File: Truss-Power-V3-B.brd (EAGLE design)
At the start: 40.3 x 20.3 mm, 41 parts, among them J1 XF2L-0625-1, U1 TPS61090, U2 MCP73831T-2ACI/OT, U3 MAX17044, U4 SN74LVC1G86DC1LR, U5 SN74LVC1G123, X1 CON-1PIN, X2 MicroB, X3 CON-1PINB, X4 CON-1PIN, X5 CON-1PIN, X6 CON-1PIN

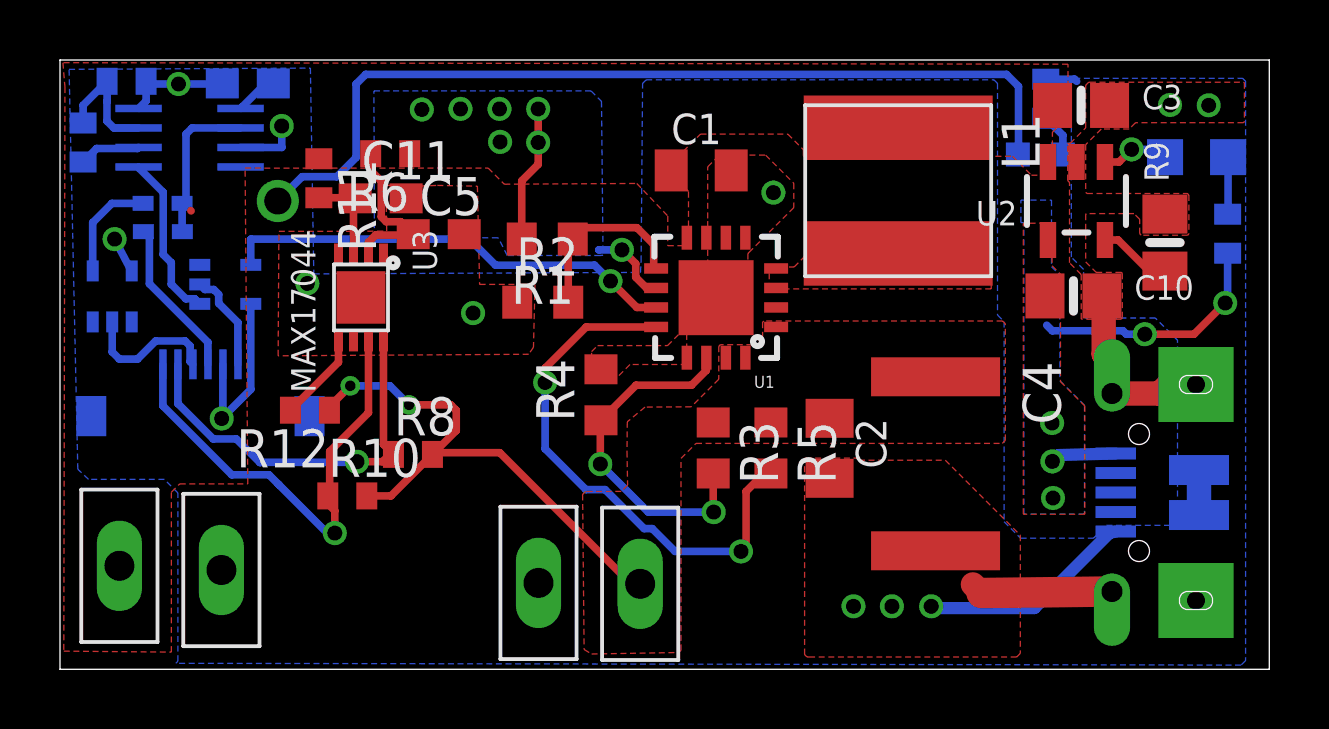
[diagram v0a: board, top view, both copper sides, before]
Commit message: Decoupling capacitor added to XOR power supply
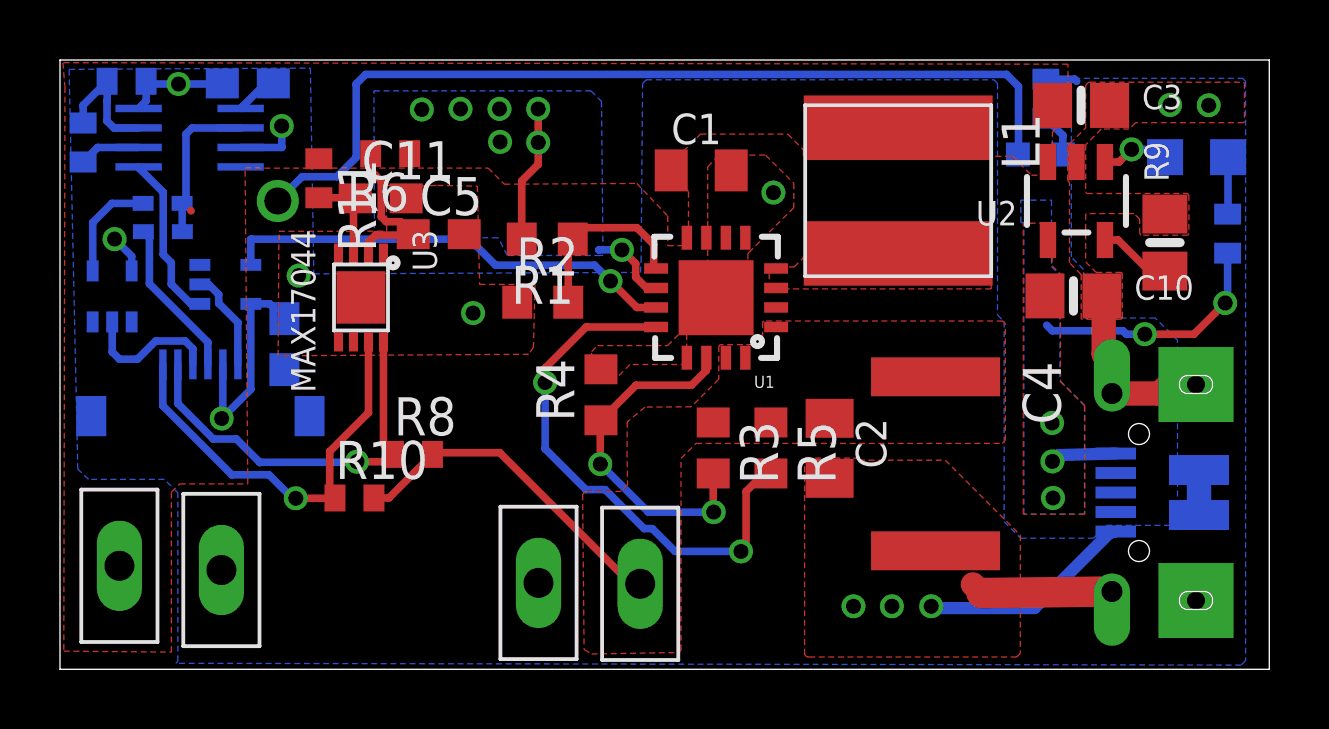
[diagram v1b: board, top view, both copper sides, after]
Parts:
- removed R12: 4.7K, resistor:R0402
- added C8: 0.1uF, rcl:C0603
- moved R10 0.25 mm to (9.82, 5.71)
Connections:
- removed net ALRT: R12.2, U3.5
- net GND: now also C8.2, U5.1, U5.4; no longer U5.P$1, U5.P$4
- net N$10: now also U5.6; no longer U5.P$6
- net N$8: now also U5.7; no longer U5.P$7
- net N$9: now also U5.2; no longer U5.P$2
- net PWR_OR_R: now also U5.5; no longer U5.P$5
- net VBAT: now also C8.1, U5.3, U5.8; no longer U5.P$3, U5.P$8
- net VCC: no longer R12.1
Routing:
- net VCC: track 18.0 -> 11.0 mm, vias 2 -> 0
- net ALRT: track 2.97 -> 0.00 mm
- net SCL: track 16.1 -> 14.2 mm
- net VBAT: track 20.3 -> 21.8 mm

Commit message: Final board files
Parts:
- R13: value 330 -> 1K
- moved C7 1.31 mm to (4.95, 19.5)
- moved R14 0.89 mm to (1.33, 19.6)
- moved C6 0.30 mm to (0.76, 17.3)
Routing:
- net VBAT: track 21.8 -> 20.5 mm
- net N$8: track 4.20 -> 3.60 mm
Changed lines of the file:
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@@
 <?xml version="1.0" encoding="utf-8"?>
 <!DOCTYPE eagle SYSTEM "eagle.dtd">
-<eagle version="8.3.2">
+<eagle version="8.4.3">
 <drawing>
 <settings>
@@
 <param name="dpMaxLengthDifference" value="10mm"/>
 <param name="dpGapFactor" value="2.5"/>
-<param name="checkGrid" value="0"/>
 <param name="checkAngle" value="0"/>
 <param name="checkFont" value="1"/>
 <param name="checkRestrict" value="0"/>
+<param name="checkStop" value="0"/>
 <param name="useDiameter" value="13"/>
 <param name="maxErrors" value="50"/>
@@
 <element name="C5" library="rcl" package="C0603" value="1uF" x="12.6238" y="14.5034"/>
 <element name="LED1" library="led" library_urn="urn:adsk.eagle:library:259" package="CHIP-LED0603" package3d_urn="urn:adsk.eagle:package:15819/1" value="" x="32.68" y="17.16" rot="MR90"/>
-<element name="R13" library="resistor" package="R0402" value="330" x="32.86" y="19.02" rot="MR270"/>
+<element name="R13" library="resistor" package="R0402" value="1K" x="32.86" y="19.02" rot="MR270"/>
 <element name="R7" library="resistor" package="R0402" value="470" x="38.92" y="14.52" rot="MR90"/>
 <element name="X4" library="NewPart" package="CON-1PIN" value="CON-1PIN" x="1.98" y="3.45" rot="R180"/>
@@
 <element name="X3" library="NewPart" package="CON-1PIN-B" value="CON-1PINB" x="7.26" y="15.61"/>
 <element name="U5" library="NewPart" package="SSOP8" value="SN74LVC1G123" x="4.32" y="17.72" rot="MR270"/>
-<element name="R14" library="resistor" package="R0402" value="10K" x="2.22" y="19.6" rot="MR0"/>
-<element name="C6" library="rcl" library_urn="urn:adsk.eagle:library:334" package="C0402" package3d_urn="urn:adsk.eagle:package:23626/1" value="1000pF" x="0.77" y="17.56" rot="MR270"/>
-<element name="C7" library="rcl" library_urn="urn:adsk.eagle:library:334" package="C0603" package3d_urn="urn:adsk.eagle:package:23616/2" value="0.1uF" x="6.26" y="19.53" rot="MR180"/>
+<element name="R14" library="resistor" package="R0402" value="10K" x="1.33" y="19.56" rot="MR0"/>
+<element name="C6" library="rcl" library_urn="urn:adsk.eagle:library:334" package="C0402" package3d_urn="urn:adsk.eagle:package:23626/1" value="1000pF" x="0.76" y="17.26" rot="MR270"/>
+<element name="C7" library="rcl" library_urn="urn:adsk.eagle:library:334" package="C0603" package3d_urn="urn:adsk.eagle:package:23616/2" value="0.1uF" x="4.95" y="19.49" rot="MR180"/>
 <element name="C8" library="rcl" library_urn="urn:adsk.eagle:library:334" package="C0603" package3d_urn="urn:adsk.eagle:package:23616/2" value="0.1uF" x="7.48" y="10.84" rot="MR270"/>
 </elements>
@@
 <wire x1="6.02" y1="18.695" x2="6.0756" y2="18.7506" width="0.254" layer="16"/>
 <wire x1="6.0756" y1="18.7506" x2="6.07573125" y2="18.7506" width="0.254" layer="16"/>
-<wire x1="6.85513125" y1="19.53" x2="7.11" y2="19.53" width="0.254" layer="16"/>
-<wire x1="6.07573125" y1="18.7506" x2="6.85513125" y2="19.53" width="0.254" layer="16"/>
 <contactref element="C8" pad="2"/>
+<wire x1="5.8" y1="19.49" x2="5.8" y2="18.915" width="0.254" layer="16"/>
+<wire x1="5.8" y1="18.915" x2="6.02" y2="18.695" width="0.254" layer="16"/>
 </signal>
 <signal name="N$14">
@@
 <contactref element="X4" pad="P$1"/>
 <contactref element="J1" pad="2"/>
-<via x="5.39" y="8.36" extent="1-16" drill="0.5"/>
+<via x="5.58" y="8.85" extent="1-16" drill="0.5"/>
 <contactref element="U$16" pad="5"/>
 <via x="1.82" y="14.34" extent="1-16" drill="0.5"/>
@@
 <contactref element="R14" pad="1"/>
 <contactref element="C7" pad="1"/>
-<wire x1="5.43" y1="8.4" x2="5.43" y2="10.165" width="0.254" layer="16"/>
-<wire x1="5.43" y1="8.4" x2="5.39" y2="8.36" width="0.254" layer="16"/>
 <wire x1="2.36" y1="13.31" x2="2.39" y2="13.28" width="0.254" layer="16"/>
-<wire x1="6.36" y1="9.33" x2="6.36" y2="12.18" width="0.254" layer="16"/>
-<wire x1="6.36" y1="9.33" x2="5.43" y2="8.4" width="0.254" layer="16"/>
-<wire x1="2.98" y1="19.49" x2="2.87" y2="19.6" width="0.254" layer="16"/>
-<wire x1="2.87" y1="19.6" x2="2.87" y2="18.945" width="0.254" layer="16"/>
-<wire x1="2.87" y1="18.945" x2="2.62" y2="18.695" width="0.254" layer="16"/>
 <via x="7.39" y="18.11" extent="1-16" drill="0.5"/>
-<wire x1="2.87" y1="19.6" x2="2.96" y2="19.51" width="0.254" layer="16"/>
-<wire x1="3.95" y1="19.51" x2="2.96" y2="19.51" width="0.254" layer="16"/>
-<via x="3.95" y="19.51" extent="1-16" drill="0.5"/>
-<wire x1="5.41" y1="19.53" x2="5.39" y2="19.51" width="0.254" layer="16"/>
-<wire x1="5.39" y1="19.51" x2="3.95" y2="19.51" width="0.254" layer="16"/>
-<wire x1="6.02" y1="17.395" x2="7.395" y2="17.395" width="0.254" layer="16"/>
-<wire x1="7.395" y1="17.395" x2="7.39" y2="18.11" width="0.254" layer="16"/>
+<via x="2.91" y="19.52" extent="1-16" drill="0.5"/>
 <contactref element="C8" pad="1"/>
-<wire x1="6.36" y1="12.18" x2="6.99" y2="12.18" width="0.254" layer="16"/>
+<wire x1="6.99" y1="12.18" x2="6.36" y2="12.18" width="0.254" layer="16"/>
 <wire x1="6.99" y1="12.18" x2="7.48" y2="11.69" width="0.254" layer="16"/>
 <wire x1="2.39" y1="13.28" x2="2.39" y2="13.77" width="0.254" layer="16"/>
 <wire x1="2.39" y1="13.77" x2="1.82" y2="14.34" width="0.254" layer="16"/>
+<wire x1="1.98" y1="19.56" x2="1.98" y2="19.335" width="0.254" layer="16"/>
+<wire x1="1.98" y1="19.335" x2="2.62" y2="18.695" width="0.254" layer="16"/>
+<wire x1="2.62" y1="18.695" x2="2.62" y2="19.23" width="0.254" layer="16"/>
+<wire x1="2.62" y1="19.23" x2="2.91" y2="19.52" width="0.254" layer="16"/>
+<wire x1="2.91" y1="19.52" x2="4.07" y2="19.52" width="0.254" layer="16"/>
+<wire x1="4.07" y1="19.52" x2="4.1" y2="19.49" width="0.254" layer="16"/>
+<wire x1="6.02" y1="17.395" x2="6.955" y2="17.395" width="0.254" layer="16"/>
+<wire x1="7.39" y1="17.83" x2="7.39" y2="18.11" width="0.254" layer="16"/>
+<wire x1="6.955" y1="17.395" x2="7.39" y2="17.83" width="0.254" layer="16"/>
+<wire x1="5.43" y1="10.165" x2="5.43" y2="9" width="0.254" layer="16"/>
+<wire x1="5.58" y1="8.85" x2="5.43" y2="9" width="0.254" layer="16"/>
+<wire x1="6.36" y1="8.99" x2="6.21" y2="8.84" width="0.254" layer="16"/>
+<wire x1="6.21" y1="8.84" x2="5.59" y2="8.84" width="0.254" layer="16"/>
+<wire x1="5.59" y1="8.84" x2="5.58" y2="8.85" width="0.254" layer="16"/>
+<wire x1="6.36" y1="12.18" x2="6.36" y2="8.99" width="0.254" layer="16"/>
 </signal>
 <signal name="VBUS">
@@
 <contactref element="U4" pad="4"/>
 <via x="18.35" y="12.94" extent="1-16" drill="0.5"/>
-<wire x1="14.52" y1="13.47" x2="13.65" y2="14.34" width="0.254" layer="16"/>
+<wire x1="13.65" y1="14.34" x2="14.52" y2="13.47" width="0.254" layer="16"/>
 <wire x1="17.82" y1="13.47" x2="18.35" y2="12.94" width="0.254" layer="16"/>
 <wire x1="14.52" y1="13.47" x2="17.82" y2="13.47" width="0.254" layer="16"/>
 <wire x1="19.87" y1="12.061" x2="19.229" y2="12.061" width="0.254" layer="1"/>
 <wire x1="19.229" y1="12.061" x2="18.35" y2="12.94" width="0.254" layer="1"/>
-<wire x1="6.37" y1="14.34" x2="13.65" y2="14.34" width="0.254" layer="16"/>
-<wire x1="6.36" y1="13.48" x2="6.36" y2="14.33" width="0.254" layer="16"/>
-<wire x1="6.36" y1="14.33" x2="6.37" y2="14.34" width="0.254" layer="16"/>
+<wire x1="6.36" y1="13.48" x2="6.36" y2="13.99" width="0.254" layer="16"/>
+<wire x1="6.36" y1="13.99" x2="6.71" y2="14.34" width="0.254" layer="16"/>
+<wire x1="6.71" y1="14.34" x2="13.65" y2="14.34" width="0.254" layer="16"/>
 </signal>
 <signal name="N$6">
@@
 <contactref element="C6" pad="1"/>
 <contactref element="R14" pad="2"/>
-<wire x1="1.57" y1="18.94013125" x2="1.57" y2="19.6" width="0.254" layer="16"/>
-<wire x1="1.57" y1="18.94013125" x2="1.5656" y2="18.93573125" width="0.254" layer="16"/>
-<wire x1="1.5656" y1="18.93573125" x2="1.5656" y2="18.2744" width="0.254" layer="16"/>
-<wire x1="1.795" y1="18.045" x2="2.62" y2="18.045" width="0.254" layer="16"/>
-<wire x1="1.5656" y1="18.2744" x2="1.795" y2="18.045" width="0.254" layer="16"/>
-<wire x1="1.57" y1="19.6" x2="0.77" y2="18.8" width="0.254" layer="16"/>
-<wire x1="0.77" y1="18.8" x2="0.77" y2="18.21" width="0.254" layer="16"/>
+<wire x1="2.62" y1="18.045" x2="0.895" y2="18.045" width="0.254" layer="16"/>
+<wire x1="0.895" y1="18.045" x2="0.76" y2="17.91" width="0.254" layer="16"/>
+<wire x1="0.76" y1="17.91" x2="0.76" y2="19.48" width="0.254" layer="16"/>
+<wire x1="0.76" y1="19.48" x2="0.68" y2="19.56" width="0.254" layer="16"/>
 </signal>
 <signal name="N$10">
 <contactref element="U5" pad="6"/>
 <contactref element="C6" pad="2"/>
-<wire x1="2.62" y1="17.395" x2="1.255" y2="17.395" width="0.254" layer="16"/>
-<wire x1="1.255" y1="17.395" x2="0.77" y2="16.91" width="0.254" layer="16"/>
+<wire x1="2.62" y1="17.395" x2="1.545" y2="17.395" width="0.254" layer="16"/>
+<wire x1="1.545" y1="17.395" x2="0.76" y2="16.61" width="0.254" layer="16"/>
 </signal>
 </signals>
